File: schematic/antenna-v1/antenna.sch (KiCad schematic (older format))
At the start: 33 parts, among them J1 CONN_COAXIAL, J2 CONN_COAXIAL, J3 VCC, J4 GND, J5 RJ45, U1 MCP633, U2 MCP633

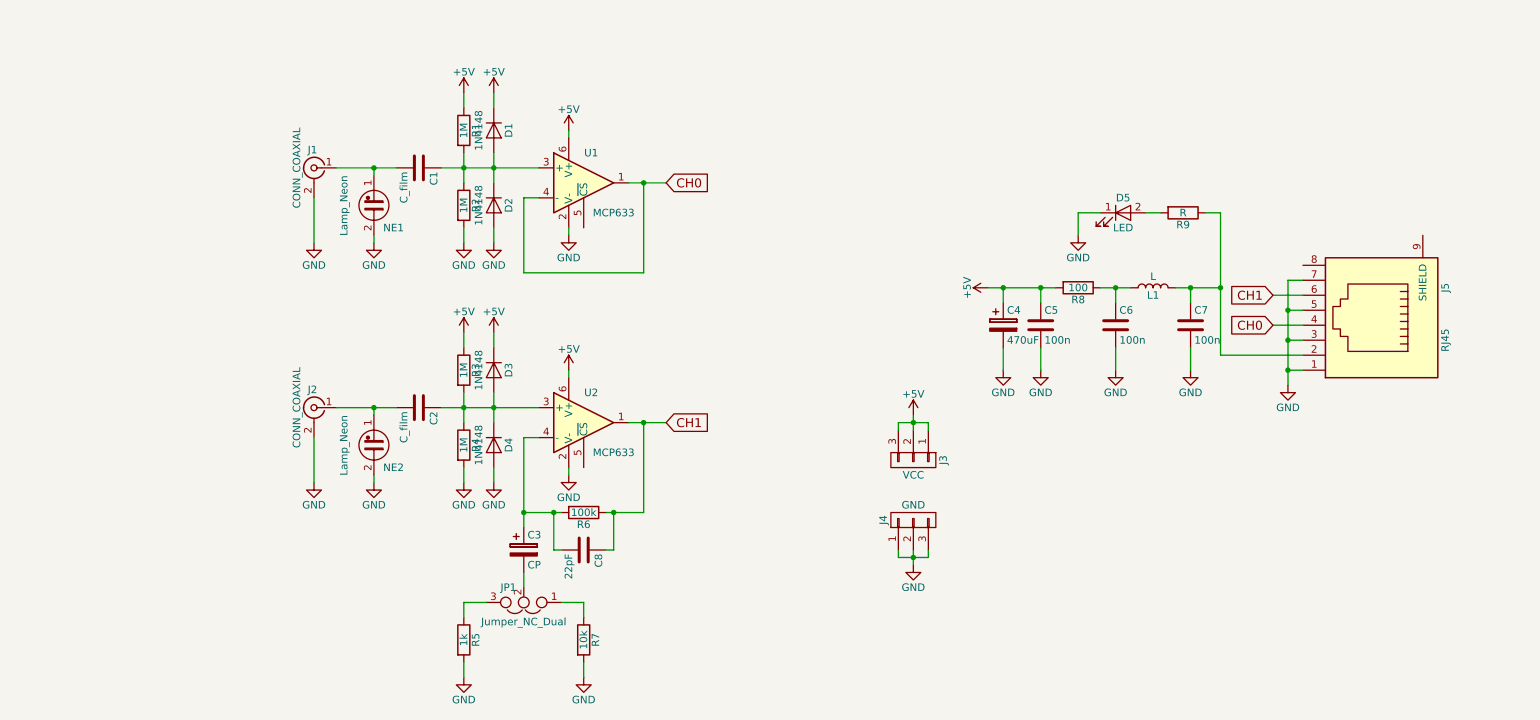
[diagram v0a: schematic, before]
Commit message: [PCB] Antenna done and input trigger output added for main device
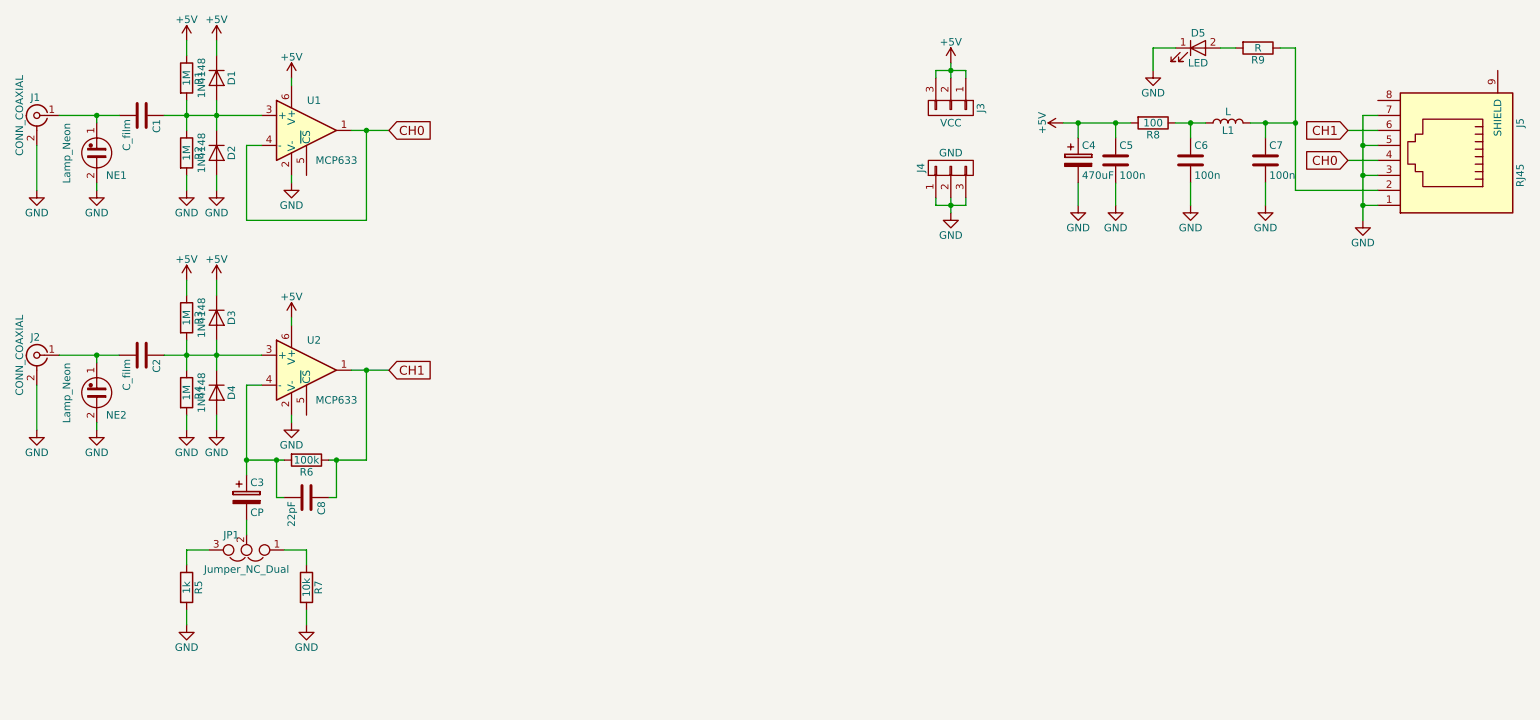
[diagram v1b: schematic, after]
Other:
- moved on the sheet: C1, C2, C3, C4, C5, C6, C7, C8, D1, D2, D3, D4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

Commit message: v1.1 PCB group done
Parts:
- removed U1, U2: MCP633, TO_SOT_Packages_SMD:SOT-23-6, symbol MCP603
- added U1, U2: MCP633, Housings_SOIC:SOIC-8_3.9x4.9mm_Pitch1.27mm, symbol CA3130
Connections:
- net +5V: now also U1.7 (V+), U2.7 (V+)
- net CH0: now also U1.2 (-), U1.6
- net CH1: now also U2.6
- net GND: now also U1.1, U1.4 (V-), U1.5, U1.8, U2.1, U2.4 (V-), U2.5, U2.8
- net at C1.1, D1.2 (A), D2.1 (K)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: now also U1.3 (+)
- net at C3.1, C8.2, R6.2: now also U2.2 (-)
- net at C2.1, D3.2 (A), D4.1 (K)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: now also U2.3 (+)
